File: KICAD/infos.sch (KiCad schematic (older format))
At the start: 0 parts

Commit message: revex with jmt
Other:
- note added: "RAF:\n> Driver de MOS\n> Recalculer la bobine et la sourcer"
- note added: "voir differentes masse avec manu\n"
- note removed: "RAF:\n> Aop Rail to Rail\n> Driver de MOS\n> Zeners du circuit de protection et autres composants\n> Recalculer la bobine et la sourcer\n> Alims\n> Revoir schema mesure de courant\n> Probleme de contre reaction négative (deuxieme switch)\n> Recalculer les ponts diviseurs avec un vref de 6V\n\n* (Régler le PID)"
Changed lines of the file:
@@
 $Descr A4 11693 8268
 encoding utf-8
-Sheet 16 16
+Sheet 7 16
 Title ""
 Date ""
@@
 $EndDescr
 Text Notes 850  7250 0    100  ~ 0
-RAF:\n> Aop Rail to Rail\n> Driver de MOS\n> Zeners du circuit de protection et autres composants\n> Recalculer la bobine et la sourcer\n> Alims\n> Revoir schema mesure de courant\n> Probleme de contre reaction négative (deuxieme switch)\n> Recalculer les ponts diviseurs avec un vref de 6V\n\n* (Régler le PID)
+RAF:\n> Driver de MOS\n> Recalculer la bobine et la sourcer
 Text Notes 3150 950  0    100  ~ 20
 Ordre soft starts: Enable Driver < PID < Entree de disjoncteur
@@
 Text Notes 9650 6250 0    50   ~ 0
 SHIELD BLOCKS\n——————————————————\nMeasure UI L + R\nDriver MOS\nRamp Generator + PID + PWM GEN\n
+Text Notes 3100 1500 0    100  ~ 0
+voir differentes masse avec manu\n
 $EndSCHEMATC

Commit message: minor cleanup
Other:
- note added: "L = Left\nR = Right\nS = Serial\nP = Parallel \nG = Gate\nD = Drain"
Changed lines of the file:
@@
 $Descr A4 11693 8268
 encoding utf-8
-Sheet 7 16
+Sheet 6 16
 Title ""
 Date ""
@@
 Text Notes 3100 1500 0    100  ~ 0
 voir differentes masse avec manu\n
+Text Notes 750  3500 0    100  ~ 0
+L = Left\nR = Right\nS = Serial\nP = Parallel \nG = Gate\nD = Drain
 $EndSCHEMATC

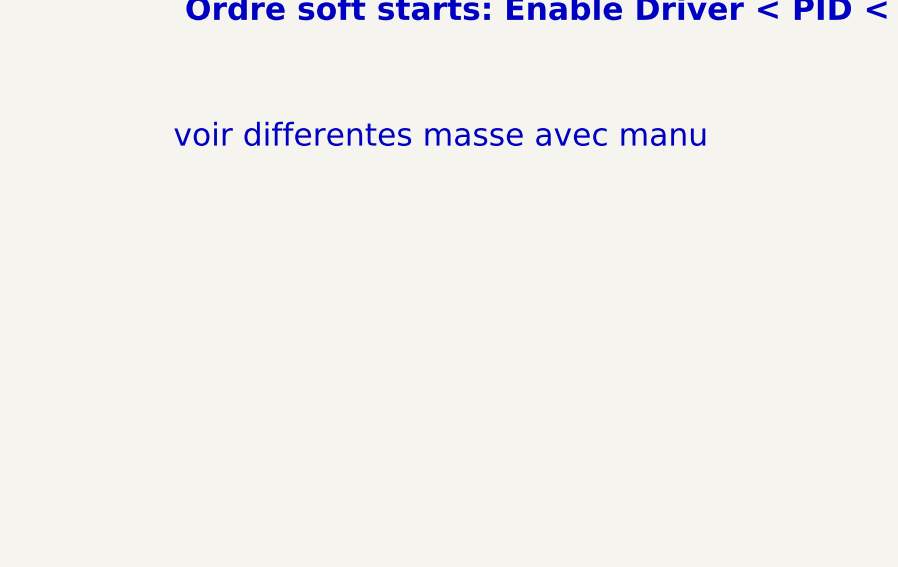
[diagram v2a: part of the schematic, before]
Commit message: drivers draft + clean and minors changes
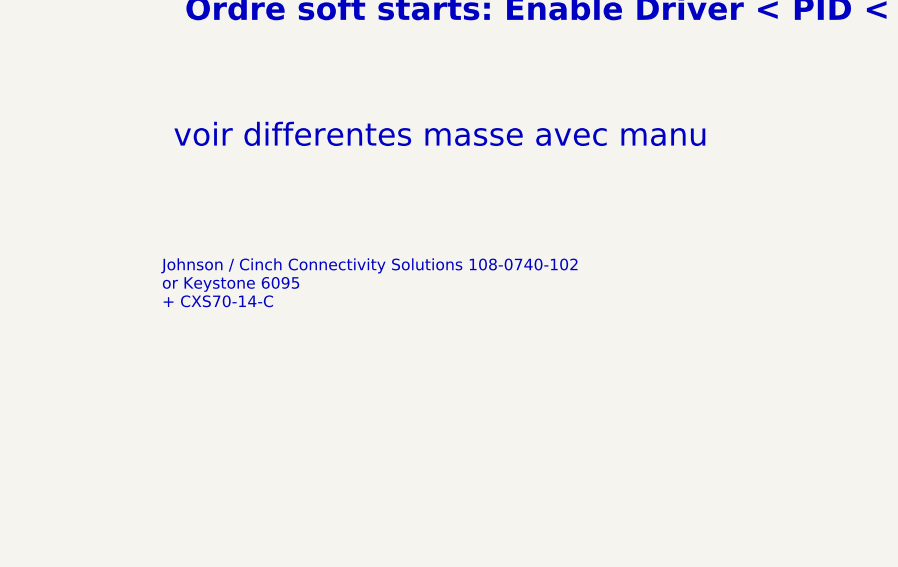
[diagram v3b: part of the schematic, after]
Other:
- note added: "Johnson / Cinch Connectivity Solutions 108-0740-102\nor Keystone 6095\n+ CXS70-14-C"
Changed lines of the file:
@@
 Text Notes 750  3500 0    100  ~ 0
 L = Left\nR = Right\nS = Serial\nP = Parallel \nG = Gate\nD = Drain
+Text Notes 3050 2200 0    50   ~ 0
+Johnson / Cinch Connectivity Solutions 108-0740-102\nor Keystone 6095\n+ CXS70-14-C
 $EndSCHEMATC

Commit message: route + work on djd
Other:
- note added: "Ordre soft starts:\nEnable Driver < PID < Entree de disjoncteur\n4.7ms < 23ms < 47ms"
- note removed: "Ordre soft starts: Enable Driver < PID < Entree de disjoncteur"
- note removed: "voir differentes masse avec manu\n"
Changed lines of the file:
@@
 Text Notes 850  7250 0    100  ~ 0
 RAF:\n> Driver de MOS\n> Recalculer la bobine et la sourcer
-Text Notes 3150 950  0    100  ~ 20
-Ordre soft starts: Enable Driver < PID < Entree de disjoncteur
+Text Notes 2750 1250 0    100  ~ 20
+Ordre soft starts:\nEnable Driver < PID < Entree de disjoncteur\n4.7ms < 23ms < 47ms
 Wire Notes Line
 	650  5400 650  7450
@@
 Text Notes 9650 6250 0    50   ~ 0
 SHIELD BLOCKS\n——————————————————\nMeasure UI L + R\nDriver MOS\nRamp Generator + PID + PWM GEN\n
-Text Notes 3100 1500 0    100  ~ 0
-voir differentes masse avec manu\n
 Text Notes 750  3500 0    100  ~ 0
 L = Left\nR = Right\nS = Serial\nP = Parallel \nG = Gate\nD = Drain

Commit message: V1.0 of the schematic
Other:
- note added: "FUTURE Improvements:\n\nSHIELD BLOCKS\n Measure UI L + R\n Driver MOS\n Ramp Generator + PID + PWM GEN\n\n——————————————————\n"
- note added: "Memo:\n L = Left\n R = Right\n S = Serial\n P = Parallel \n G = Gate\n D = Drain"
- note added: "Power connectors:\n Johnson / Cinch Connectivity Solutions 108-0740-102\n or Keystone 6095\n + CXS70-14-C"
- note added: "Soft starts order:\nEnable Driver < PID < Entree de disjoncteur\n4.7ms < 23ms < 47ms"
- note removed: "Johnson / Cinch Connectivity Solutions 108-0740-102\nor Keystone 6095\n+ CXS70-14-C"
- note removed: "L = Left\nR = Right\nS = Serial\nP = Parallel \nG = Gate\nD = Drain"
- note removed: "Ordre soft starts:\nEnable Driver < PID < Entree de disjoncteur\n4.7ms < 23ms < 47ms"
- note removed: "RAF:\n> Driver de MOS\n> Recalculer la bobine et la sourcer"
- note removed: "SHIELD BLOCKS\n——————————————————\nMeasure UI L + R\nDriver MOS\nRamp Generator + PID + PWM GEN\n"
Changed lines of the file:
@@
 $Descr A4 11693 8268
 encoding utf-8
-Sheet 6 17
-Title ""
-Date ""
-Rev ""
-Comp ""
+Sheet 5 17
+Title "SESAME"
+Date "2021-09-23"
+Rev "1"
+Comp "ALEEA"
 Comment1 ""
 Comment2 ""
@@
 Comment4 ""
 $EndDescr
-Text Notes 850  7250 0    100  ~ 0
-RAF:\n> Driver de MOS\n> Recalculer la bobine et la sourcer
-Text Notes 2750 1250 0    100  ~ 20
-Ordre soft starts:\nEnable Driver < PID < Entree de disjoncteur\n4.7ms < 23ms < 47ms
+Text Notes 650  1150 0    100  ~ 20
+Soft starts order:\nEnable Driver < PID < Entree de disjoncteur\n4.7ms < 23ms < 47ms
+Text Notes 7200 2100 0    100  ~ 20
+FUTURE Improvements:\n\nSHIELD BLOCKS\n    Measure UI L + R\n    Driver MOS\n    Ramp Generator + PID + PWM GEN\n\n——————————————————\n
+Text Notes 650  2600 0    100  ~ 20
+Memo:\n    L = Left\n    R = Right\n    S = Serial\n    P = Parallel \n    G = Gate\n    D = Drain
+Text Notes 650  3550 0    100  ~ 20
+Power connectors:\n    Johnson / Cinch Connectivity Solutions 108-0740-102\n    or Keystone 6095\n    + CXS70-14-C
 Wire Notes Line
-	650  5400 650  7450
+	11150 550  11150 6450
 Wire Notes Line
-	650  7450 5600 7450
+	11150 6450 7000 6450
 Wire Notes Line
-	5600 7450 5600 5400
+	7000 6450 7000 550
 Wire Notes Line
-	5600 5400 650  5400
-Text Notes 9650 6250 0    50   ~ 0
-SHIELD BLOCKS\n——————————————————\nMeasure UI L + R\nDriver MOS\nRamp Generator + PID + PWM GEN\n
-Text Notes 750  3500 0    100  ~ 0
-L = Left\nR = Right\nS = Serial\nP = Parallel \nG = Gate\nD = Drain
-Text Notes 3050 2200 0    50   ~ 0
-Johnson / Cinch Connectivity Solutions 108-0740-102\nor Keystone 6095\n+ CXS70-14-C
+	7000 550  11150 550
 $EndSCHEMATC
